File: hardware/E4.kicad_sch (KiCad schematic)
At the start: 0 parts

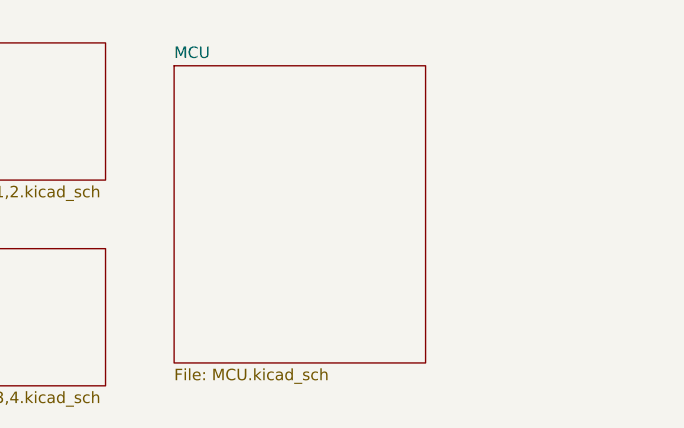
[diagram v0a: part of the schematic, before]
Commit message: feat：输入滤波原理图
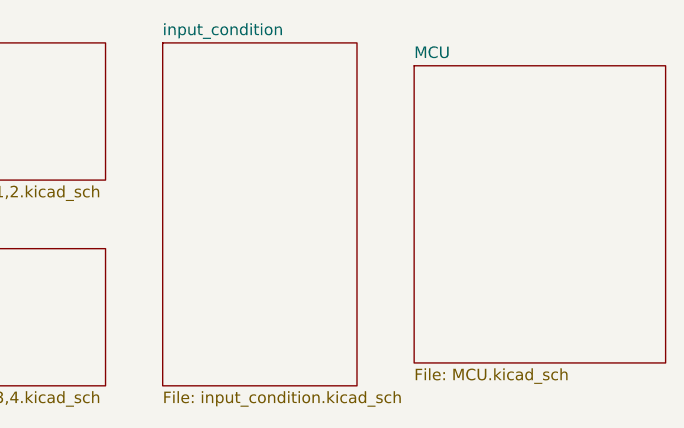
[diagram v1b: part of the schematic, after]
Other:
- added sheet input_condition (input_condition.kicad_sch)
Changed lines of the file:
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@@
 	)
 	(sheet
-		(at 69.85 35.56)
+		(at 68.58 33.02)
+		(size 21.59 38.1)
+		(exclude_from_sim no)
+		(in_bom yes)
+		(on_board yes)
+		(dnp no)
+		(fields_autoplaced yes)
+		(stroke
+			(width 0.1524)
+			(type solid)
+		)
+		(fill
+			(color 0 0 0 0)
+		)
+		(property "Sheetname" "input_condition"
+			(at 68.58 32.3084 0)
+			(show_name no)
+			(do_not_autoplace no)
+			(effects
+				(font
+					(size 1.27 1.27)
+				)
+				(justify left bottom)
+			)
+		)
+		(property "Sheetfile" "input_condition.kicad_sch"
+			(at 68.58 71.7046 0)
+			(show_name no)
+			(do_not_autoplace no)
+			(effects
+				(font
+					(size 1.27 1.27)
+				)
+				(justify left top)
+			)
+		)
+		(instances
+			(project "E4"
+				(path "/7664cc8d-15c4-46a0-b3f4-8b4373008b19"
+					(page "4")
+				)
+			)
+		)
+	)
+	(sheet
+		(at 96.52 35.56)
 		(size 27.94 33.02)
 		(exclude_from_sim no)
@@
 		)
 		(property "Sheetname" "MCU"
-			(at 69.85 34.8484 0)
+			(at 96.52 34.8484 0)
 			(show_name no)
 			(do_not_autoplace no)
@@
 		)
 		(property "Sheetfile" "MCU.kicad_sch"
-			(at 69.85 69.1646 0)
+			(at 96.52 69.1646 0)
 			(show_name no)
 			(do_not_autoplace no)
@@
 		)
 		(property "Field2" ""
-			(at 69.85 35.56 0)
+			(at 96.52 35.56 0)
 			(hide yes)
 			(show_name no)

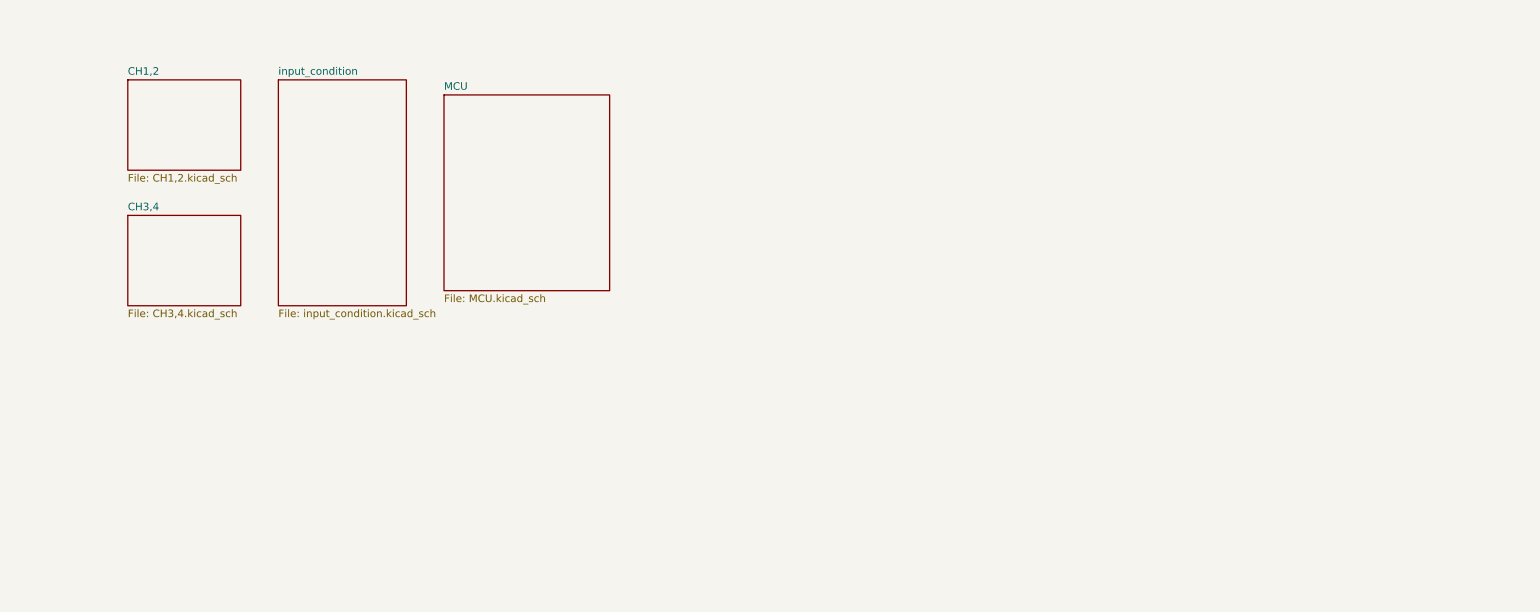
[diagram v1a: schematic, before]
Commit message: feat：电平触发原理图
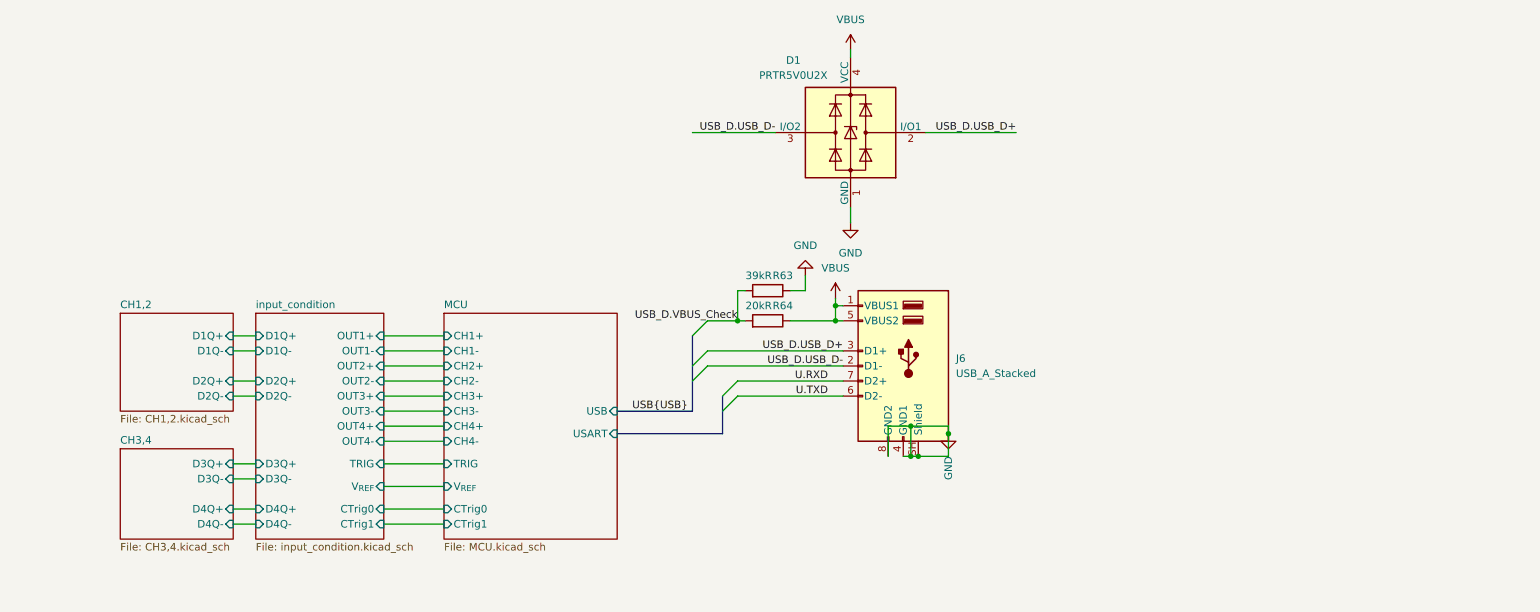
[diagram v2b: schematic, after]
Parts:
- added D1: PRTR5V0U2X, Package_TO_SOT_SMD:SOT-143, symbol Power_Protection:PRTR5V0U2X
- added J6: USB_A_Stacked, symbol Connector:USB_A_Stacked
- added R63: 39kR, Resistor_SMD:R_0603_1608Metric, symbol Device:R
- added R64: 20kR, Resistor_SMD:R_0603_1608Metric, symbol Device:R
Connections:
- new net GND: D1.1 (GND), J6.4 (GND1), J6.8 (GND2), J6.SH (Shield), R63.1
- new net U.RXD: J6.7 (D2+)
- new net U.TXD: J6.6 (D2-)
- new net USB_D.USB_D+: D1.2 (I/O1), J6.3 (D1+)
- new net USB_D.USB_D-: D1.3 (I/O2), J6.2 (D1-)
- new net USB_D.VBUS_Check: R63.2, R64.2
- new net VBUS: D1.4 (VCC), J6.1 (VBUS1), J6.5 (VBUS2), R64.1
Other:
- sheet CH1,2 ports: added D1Q+, D1Q-, D2Q+, D2Q-; removed none
- sheet CH3,4 ports: added D3Q+, D3Q-, D4Q+, D4Q-; removed none
- sheet MCU ports: added CH1+, CH1-, CH2+, CH2-, CH3+, CH3-, CH4+, CH4-, CTrig0, CTrig1, TRIG, USART, USB, V_{REF}; removed none
- sheet input_condition ports: added CTrig0, CTrig1, D1Q+, D1Q-, D2Q+, D2Q-, D3Q+, D3Q-, D4Q+, D4Q-, OUT1+, OUT1-, OUT2+, OUT2-, OUT3+, OUT3-, OUT4+, OUT4-, TRIG, V_{REF}; removed none

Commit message: feat：电源原理图
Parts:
- added J7: Barrel_Jack_Switch, Connector_BarrelJack:BarrelJack_Kycon_KLDX-0202-xC_Horizontal, symbol Connector:Barrel_Jack_Switch
- added SW2: PS-22F02, Button_Switch_THT:SW-TH_G-SWITCH-PS-22F03N, symbol Switch:PS-22F02
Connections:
- net GND: now also J7.2, J7.3, SW2.7, SW2.8
- net VBUS: now also SW2.3 (C), SW2.4 (A)
- new net VCC: SW2.2 (B), SW2.5 (B)
- new net V_{IN}: J7.1, SW2.1 (A), SW2.6 (C)
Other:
- added sheet power (power.kicad_sch)
- sheet input_condition ports: added none; removed V_{REF}
- moved on the sheet: D1, J6, R63, R64

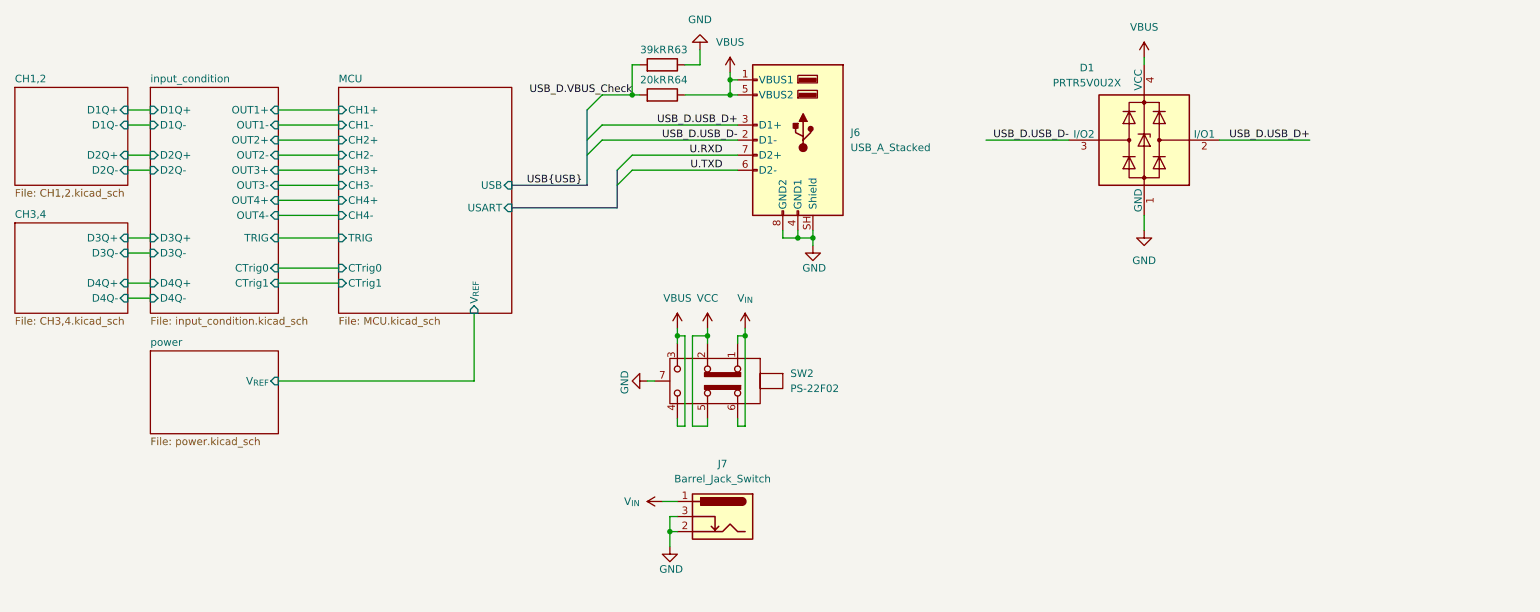
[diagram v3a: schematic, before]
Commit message: feat：模拟前端布线，单片机/SRAM布线
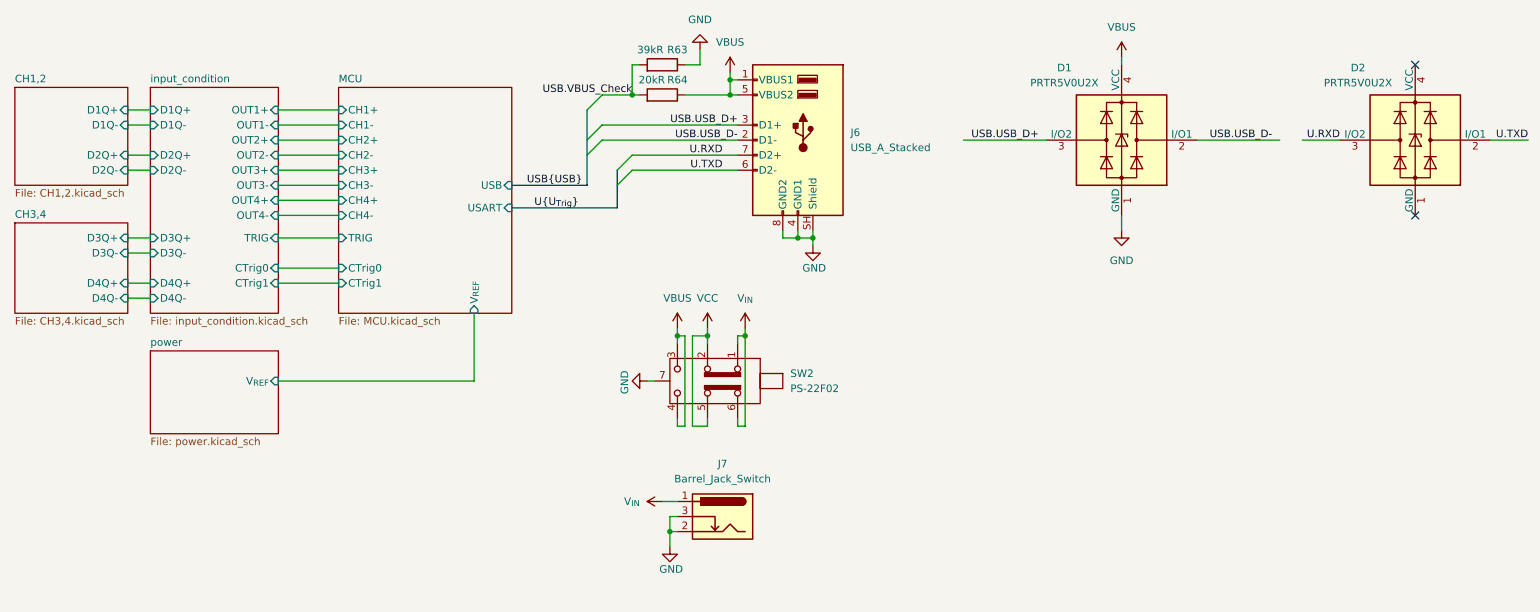
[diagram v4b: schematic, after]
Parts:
- added D2: PRTR5V0U2X, Package_TO_SOT_SMD:SOT-143, symbol Power_Protection:PRTR5V0U2X
- J6: footprint (none) -> Connector_USB:USB_A_CUI_UJ2-ADH-TH_Horizontal_Stacked
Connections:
- net U.RXD: now also D2.3 (I/O2)
- net U.TXD: now also D2.2 (I/O1)
- net USB_D.USB_D+ renamed USB.USB_D+
- net USB.USB_D+: now also D1.3 (I/O2); no longer D1.2 (I/O1)
- net USB_D.USB_D- renamed USB.USB_D-
- net USB.USB_D-: now also D1.2 (I/O1); no longer D1.3 (I/O2)
- net USB_D.VBUS_Check renamed USB.VBUS_Check
- no-connect marks 0 -> 2
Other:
- moved on the sheet: D1

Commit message: feat：电源部分
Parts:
- added D3: SMBJ5A, Diode_SMD:D_SMF, symbol Diode:SMBJ5A
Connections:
- net GND: now also D2.1 (GND), D3.2 (A2)
- net U.RXD: now also D2.2 (I/O1), J6.3 (D1+); no longer D2.3 (I/O2), J6.7 (D2+)
- net U.TXD: now also D2.3 (I/O2), J6.2 (D1-); no longer D2.2 (I/O1), J6.6 (D2-)
- net USB.USB_D+: now also D1.2 (I/O1), J6.7 (D2+); no longer D1.3 (I/O2), J6.3 (D1+)
- net USB.USB_D-: now also D1.3 (I/O2), J6.6 (D2-); no longer D1.2 (I/O1), J6.2 (D1-)
- net VBUS: now also D2.4 (VCC)
- net V_{IN}: now also D3.1 (A1)
- no-connect marks 2 -> 0
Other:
- sheet CH1,2 ports: added Ctrl1, Ctrl2; removed none
- sheet CH3,4 ports: added Ctrl3, Ctrl4; removed none
- sheet MCU ports: added Ctrl1, Ctrl2, Ctrl3, Ctrl4; removed none

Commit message: feat：总体连接
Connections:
- net USB.VBUS_Check renamed USB.USB_Check
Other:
- sheet MCU ports: added V_{REF_OUT}; removed V_{REF}
- sheet power ports: added V_{REF_OUT}; removed V_{REF}
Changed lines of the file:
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@@
 		)
 	)
-	(label "USB.VBUS_Check"
+	(label "USB.USB_Check"
 		(at 128.27 35.56 180)
 		(effects
@@
 			)
 		)
-		(pin "V_{REF}" input
-			(at 101.6 72.39 270)
-			(effects
-				(font
-					(size 1.27 1.27)
-				)
-				(justify left)
-			)
-		)
 		(pin "CTrig0" input
 			(at 78.74 64.77 180)
@@
 		(pin "Ctrl4" input
 			(at 93.98 72.39 270)
+			(effects
+				(font
+					(size 1.27 1.27)
+				)
+				(justify left)
+			)
+		)
+		(pin "V_{REF_OUT}" input
+			(at 101.6 72.39 270)
 			(effects
 				(font
@@
 			)
 		)
-		(pin "V_{REF}" input
+		(pin "V_{REF_OUT}" input
 			(at 68.58 83.82 0)
 			(effects
